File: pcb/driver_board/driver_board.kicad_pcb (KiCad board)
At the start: 2 copper layers, 33 parts

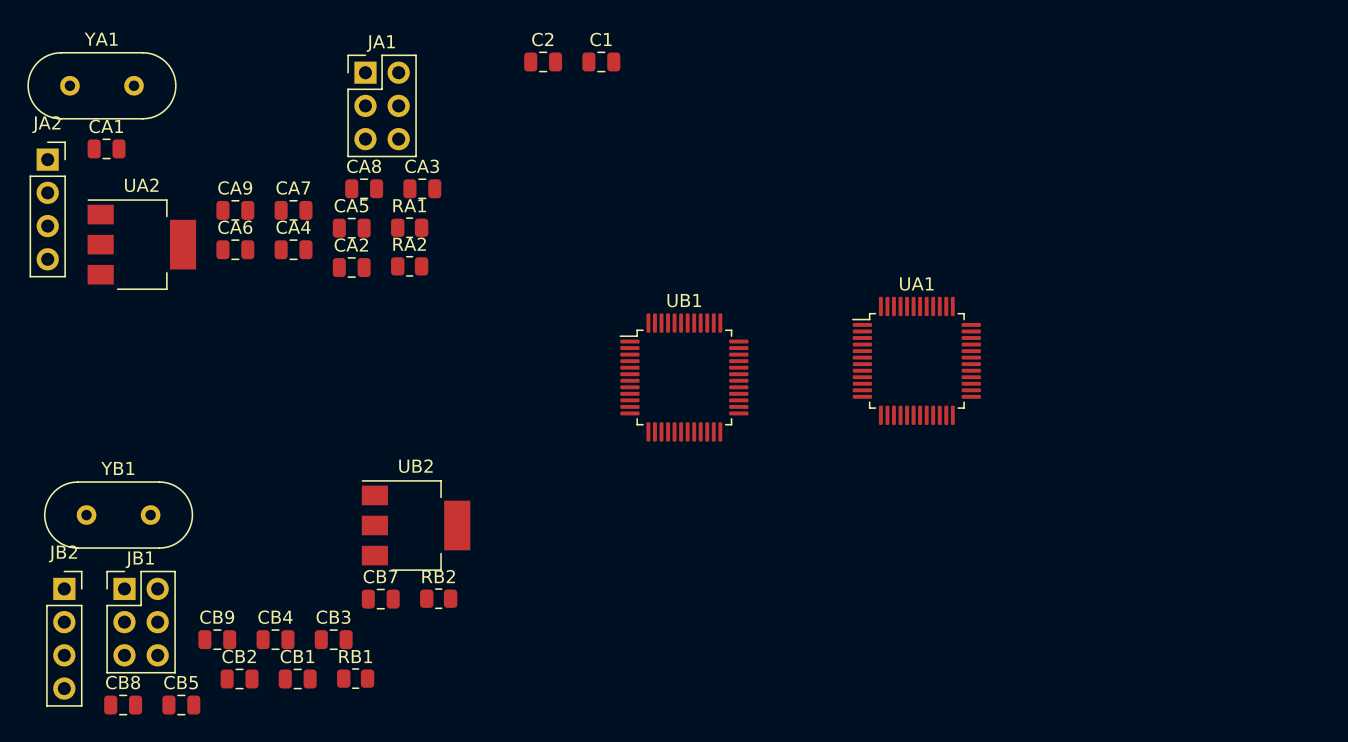
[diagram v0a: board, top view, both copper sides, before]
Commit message: Update Power supply scheme.
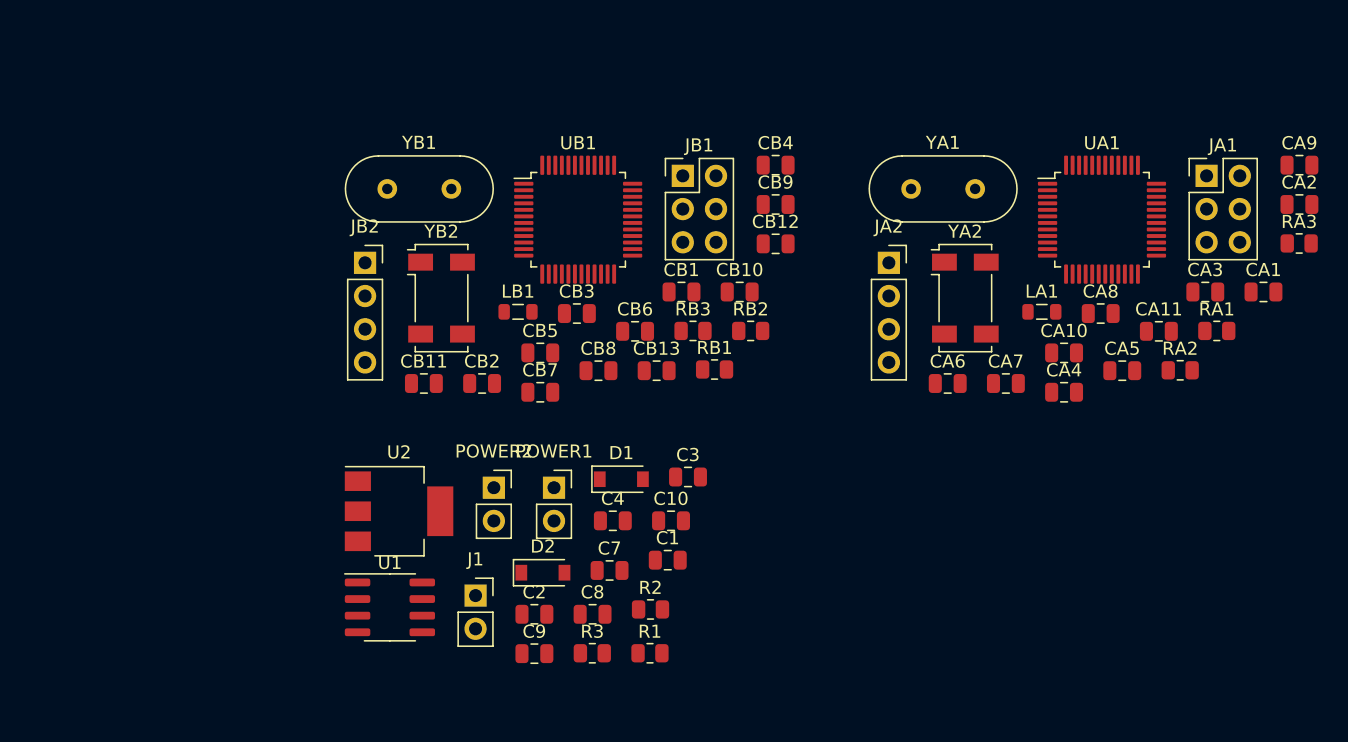
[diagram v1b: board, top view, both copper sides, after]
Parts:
- removed UA2, UB2: AMS1117-3.3, Package_TO_SOT_SMD:SOT-223-3_TabPin2
- added C10: 0.1uF, Capacitor_SMD:C_0805_2012Metric, F.Cu at (100.6, 80.8)
- added C3: 22pF, Capacitor_SMD:C_0805_2012Metric, F.Cu at (101.9, 77.5)
- added C4: 22pF, Capacitor_SMD:C_0805_2012Metric, F.Cu at (96.1, 80.8)
- added C7: 10uF, Capacitor_SMD:C_0805_2012Metric, F.Cu at (95.9, 84.6)
- added C8: 0.1uF, Capacitor_SMD:C_0805_2012Metric, F.Cu at (94.6, 88.0)
- added C9: 10uF, Capacitor_SMD:C_0805_2012Metric, F.Cu at (90.1, 91.0)
- added CA10: 20pF, Capacitor_SMD:C_0805_2012Metric, F.Cu at (130.6, 68.0)
- added CA11: 20pF, Capacitor_SMD:C_0805_2012Metric, F.Cu at (137.9, 66.3)
- added CB10: 20pF, Capacitor_SMD:C_0805_2012Metric, F.Cu at (105.8, 63.3)
- added CB11: 20pF, Capacitor_SMD:C_0805_2012Metric, F.Cu at (81.7, 70.3)
- added CB12: 1uF, Capacitor_SMD:C_0805_2012Metric, F.Cu at (108.6, 59.6)
- added CB13: 10nF, Capacitor_SMD:C_0805_2012Metric, F.Cu at (99.5, 69.3)
- added CB6: 0.1uF, Capacitor_SMD:C_0805_2012Metric, F.Cu at (97.8, 66.3)
- added D1: 1N5817, Diode_SMD:D_SOD-123, F.Cu at (96.8, 77.6)
- added D2: 1N5817, Diode_SMD:D_SOD-123, F.Cu at (90.8, 84.8)
- added J1: Conn_01x02, Connector_PinSocket_2.54mm:PinSocket_1x02_P2.54mm_Vertical, F.Cu at (85.6, 86.5)
- added LA1: 10uH, Inductor_SMD:L_0805_2012Metric, F.Cu at (128.9, 64.8)
- added LB1: 10uH, Inductor_SMD:L_0805_2012Metric, F.Cu at (88.9, 64.8)
- added POWER1: Conn_01x02, Connector_PinSocket_2.54mm:PinSocket_1x02_P2.54mm_Vertical, F.Cu at (91.6, 78.3)
- added POWER2: Conn_01x02, Connector_PinSocket_2.54mm:PinSocket_1x02_P2.54mm_Vertical, F.Cu at (87.0, 78.3)
- added R1: 33R, Resistor_SMD:R_0805_2012Metric, F.Cu at (99.0, 90.9)
- added R2: 33R, Resistor_SMD:R_0805_2012Metric, F.Cu at (99.0, 87.6)
- added R3: 120R, Resistor_SMD:R_0805_2012Metric, F.Cu at (94.6, 90.9)
- added RA3: 0R, Resistor_SMD:R_0805_2012Metric, F.Cu at (148.6, 59.6)
- added RB3: 0R, Resistor_SMD:R_0805_2012Metric, F.Cu at (102.3, 66.3)
- added U1: TJA1051T, Package_SO:SOIC-8_3.9x4.9mm_P1.27mm, F.Cu at (79.1, 87.4)
- added U2: AMS1117-3.3, Package_TO_SOT_SMD:SOT-223-3_TabPin2, F.Cu at (79.8, 80.1)
- added YA2: 32768HZ, Crystal:Crystal_SMD_Abracon_ABS25-4Pin_8.0x3.8mm, F.Cu at (123.1, 63.8)
- added YB2: 32768HZ, Crystal:Crystal_SMD_Abracon_ABS25-4Pin_8.0x3.8mm, F.Cu at (83.0, 63.8)
- CA1: value 10uF -> 4.7uF
- CA2: value 0.1uF -> 10nF
- CA6: value 0.1uF -> 1uF
- CB1: value 10uF -> 0.1uF
- CB2: value 0.1uF -> 4.7uF
- YB1: value 8M -> 8MHZ
- moved CA1 89.2 mm to (145.9, 63.3)
- moved CA9 81.5 mm to (148.6, 53.6)
- moved CA2 72.6 mm to (148.6, 56.6)
- moved JA1 64.8 mm to (141.5, 54.4)
- moved JA2 64.8 mm to (117.2, 61.1)
- moved YA1 64.8 mm to (118.9, 55.4)
- moved RA1 62.2 mm to (142.3, 66.3)
- moved CA3 60.4 mm to (141.4, 63.3)
- moved CA5 59.9 mm to (135.1, 69.3)
- moved CA4 59.9 mm to (130.6, 71.0)
- moved RA2 59.5 mm to (139.5, 69.3)
- moved CA8 57.1 mm to (133.4, 65.0)
- moved CA7 56.1 mm to (126.2, 70.3)
- moved CA6 55.4 mm to (121.7, 70.3)
- moved CB9 54.1 mm to (108.6, 56.6)
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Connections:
- net /Sheet6121200E/OSC_IN renamed /Sheet6121200E/RCC_OSC_IN
- net /Sheet6121200E/OSC_OUT renamed /Sheet6121200E/RCC_OSC_OUT
- net /Sheet6121200E/SWCL renamed /Sheet6121200E/SYS_JTCK-SWCL
- net /Sheet6121200E/SWDIO renamed /Sheet6121200E/SYS_JTMS-SWDIO
- net /sheet61233186/OSC_IN renamed /sheet61233186/RCC_OSC_IN
- net /sheet61233186/OSC_OUT renamed /sheet61233186/RCC_OSC_OUT
- net /sheet61233186/SWCL renamed /sheet61233186/SYS_JTCK-SWCL
- net /sheet61233186/SWDIO renamed /sheet61233186/SYS_JTMS-SWDIO
- net Net-(UA1-Pad42) renamed /Sheet6121200E/USART1_TX
- net Net-(UA1-Pad43) renamed /Sheet6121200E/USART1_RX
- net VCC renamed +5V
- CA1 pad 1: /Sheet6121200E/V3.3 -> /Sheet6121200E/VDD1
- CA2 pad 1: /Sheet6121200E/V3.3 -> +3.3VA
- CA3 pad 1: /Sheet6121200E/V3.3 -> /Sheet6121200E/VDD1
- CA4 pad 1: /Sheet6121200E/V3.3 -> /Sheet6121200E/VDD1
- CA5 pad 1: /Sheet6121200E/V3.3 -> /Sheet6121200E/VDD1
- CA6 pad 1: /Sheet6121200E/V3.3 -> +3.3VA
- CA9 pad 1: /Sheet6121200E/V3.3 -> +3.3V
- CB1 pad 1: /sheet61233186/V3.3 -> /sheet61233186/VDD1
- CB2 pad 1: /sheet61233186/V3.3 -> /sheet61233186/VDD2
- CB3 pad 1: /sheet61233186/V3.3 -> +3.3V
- CB4 pad 1: /sheet61233186/V3.3 -> +3.3V
- CB5 pad 1: /sheet61233186/V3.3 -> +3.3V
- CB9 pad 1: /sheet61233186/V3.3 -> +3.3V
- JA1 pad 1: /Sheet6121200E/V3.3 -> +3.3V
- JA1 pad 2: /Sheet6121200E/V3.3 -> +3.3V
- JA2 pad 4: /Sheet6121200E/V3.3 -> +3.3V
- JB1 pad 1: /sheet61233186/V3.3 -> +3.3V
- JB1 pad 2: /sheet61233186/V3.3 -> +3.3V
- JB2 pad 4: /sheet61233186/V3.3 -> +3.3V
- UA1 pad 12: Net-(UA1-Pad12) -> /sheet61233186/F031_RX
- UA1 pad 13: Net-(UA1-Pad13) -> /sheet61233186/F031_TX
- UA1 pad 24: /Sheet6121200E/V3.3 -> /Sheet6121200E/VDD1
- UA1 pad 3: Net-(UA1-Pad3) -> /Sheet6121200E/RCC_OSC32_IN
- UA1 pad 30: /sheet61233186/F031_RX -> Net-(UA1-Pad30)
- UA1 pad 31: /sheet61233186/F031_TX -> Net-(UA1-Pad31)
- UA1 pad 36: /Sheet6121200E/V3.3 -> /Sheet6121200E/VDD1
- UA1 pad 4: Net-(UA1-Pad4) -> /Sheet6121200E/RCC_OSC32_OUT
- UA1 pad 45: Net-(UA1-Pad45) -> CAN_RX
- UA1 pad 46: Net-(UA1-Pad46) -> CAN_TX
- UA1 pad 48: /Sheet6121200E/V3.3 -> /Sheet6121200E/VDD1
- UA1 pad 8: GND -> GNDA
- UA1 pad 9: /Sheet6121200E/V3.3 -> +3.3VA
- UB1 pad 24: /sheet61233186/V3.3 -> /sheet61233186/VDD1
- UB1 pad 3: Net-(UB1-Pad3) -> /sheet61233186/RCC_OSC32_IN
- UB1 pad 4: Net-(UB1-Pad4) -> /sheet61233186/RCC_OSC32_OUT
- UB1 pad 48: /sheet61233186/V3.3 -> /sheet61233186/VDD2
- UB1 pad 8: GND -> GNDA
- UB1 pad 9: /sheet61233186/V3.3 -> +3.3VA

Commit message: Update layout.
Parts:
- removed CA1: 4.7uF, Capacitor_SMD:C_0805_2012Metric
- removed CA10, CA11, CA7, CA8, CB11: 20pF, Capacitor_SMD:C_0805_2012Metric
- removed CA2, CB13: 10nF, Capacitor_SMD:C_0805_2012Metric
- removed CA3, CA4, CA5, CA9: 0.1uF, Capacitor_SMD:C_0805_2012Metric
- removed CA6, CB12: 1uF, Capacitor_SMD:C_0805_2012Metric
- removed J1: Conn_01x02, Connector_PinSocket_2.54mm:PinSocket_1x02_P2.54mm_Vertical
- removed JA1: Conn_02x03_Odd_Even, Connector_PinHeader_2.54mm:PinHeader_2x03_P2.54mm_Vertical
- removed JA2: Conn_01x04, Connector_PinSocket_2.54mm:PinSocket_1x04_P2.54mm_Vertical
- removed LA1: 10uH, Inductor_SMD:L_0805_2012Metric
- removed RA1, RA2: 100K, Resistor_SMD:R_0805_2012Metric
- removed RA3: 0R, Resistor_SMD:R_0805_2012Metric
- removed UA1: STM32F103C6Tx, Package_QFP:LQFP-48_7x7mm_P0.5mm
- removed YA1: 8M, Crystal:Crystal_HC18-U_Vertical
- removed YA2: 32768HZ, Crystal:Crystal_SMD_Abracon_ABS25-4Pin_8.0x3.8mm
- added C11: 10pF, Capacitor_SMD:C_0805_2012Metric, F.Cu at (83.8, 129.9)
- added CAN1: Conn_01x02, Connector_Phoenix_MC:PhoenixContact_MCV_1,5_2-G-3.81_1x02_P3.81mm_Vertical, F.Cu at (119.4, 132.7)
- added LED1: LED, LED_SMD:LED_0805_2012Metric, F.Cu at (99.7, 126.0)
- added Motor1: Conn_01x05, Connector_PinHeader_2.54mm:PinHeader_1x05_P2.54mm_Vertical, F.Cu at (78.7, 43.2)
- added Motor2: Conn_01x05, Connector_PinHeader_2.54mm:PinHeader_1x05_P2.54mm_Vertical, F.Cu at (78.7, 58.4)
- added Motor3: Conn_01x05, Connector_PinHeader_2.54mm:PinHeader_1x05_P2.54mm_Vertical, F.Cu at (78.7, 73.7)
- added R4: 10K, Resistor_SMD:R_0805_2012Metric, F.Cu at (80.6, 127.9)
- added R5: 510R, Resistor_SMD:R_0805_2012Metric, F.Cu at (99.7, 122.2)
- added SW1: SW_Push, Button_Switch_SMD:SW_SPST_B3U-1000P, F.Cu at (80.6, 132.5)
- CB1, CB2, CB3, LB1, RB3: moved to B.Cu
- CB4: value 0.1uF -> 1uF; moved to B.Cu
- CB5: value 0.1uF -> 10nF; moved to B.Cu
- CB6, CB9: value 0.1uF -> 20pF
- CB8: value 20pF -> 0.1uF
- POWER1, POWER2: footprint Connector_PinSocket_2.54mm:PinSocket_1x02_P2.54mm_Vertical -> Connector_Phoenix_MC:PhoenixContact_MCV_1,5_2-G-3.81_1x02_P3.81mm_Vertical
- moved POWER1 56.2 mm to (105.4, 132.7)
- moved POWER2 54.5 mm to (89.5, 132.7)
- moved RB2 54.3 mm to (157.8, 84.5)
- moved CB6 52.8 mm to (147.8, 83.2)
- moved D2 51.4 mm to (124.2, 123.8), turned to 180 degrees
- moved D1 51.0 mm to (118.4, 123.8)
- moved CB8 50.5 mm to (141.5, 89.2)
- moved RB1 46.5 mm to (145.9, 89.2)
- moved YB2 46.5 mm to (125.0, 83.7)
- moved YB1 45.8 mm to (124.5, 50.8)
- moved U1 45.6 mm to (121.3, 104.8), turned to 270 degrees
- moved CB10 44.8 mm to (144.3, 86.2)
- moved U2 43.9 mm to (107.3, 114.3), turned to 90 degrees
- moved C4 43.8 mm to (123.2, 115.2), turned to 270 degrees
- moved CB9 43.3 mm to (137.0, 89.2)
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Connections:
- C4 pad 1: /CANL -> /CANH
- C7 pad 2: GND -> GNDA
- C8 pad 2: GND -> GNDA
- CB1 pad 1: /sheet61233186/VDD1 -> +3.3V
- CB10 pad 2: /sheet61233186/RCC_OSC32_IN -> /sheet61233186/RCC_OSC32_OUT
- CB2 pad 1: /sheet61233186/VDD2 -> +3.3V
- CB4 pad 1: +3.3V -> +3.3VA
- CB5 pad 1: +3.3V -> +3.3VA
- CB6 pad 1: /sheet61233186/VDD2 -> Net-(CB6-Pad1)
- CB6 pad 2: GND -> /sheet61233186/RCC_OSC_IN
- CB7 pad 1: Net-(CB7-Pad1) -> Net-(CB6-Pad1)
- CB7 pad 2: /sheet61233186/RCC_OSC_IN -> /sheet61233186/RCC_OSC_OUT
- CB8 pad 1: Net-(CB7-Pad1) -> +3.3V
- CB8 pad 2: /sheet61233186/RCC_OSC_OUT -> Net-(CB8-Pad2)
- CB9 pad 1: +3.3V -> Net-(CB10-Pad1)
- CB9 pad 2: GND -> /sheet61233186/RCC_OSC32_IN
- JB2 pad 1: GND -> Net-(CB8-Pad2)
- POWER2 pad 1: GND -> GNDA
- UB1 pad 11: Net-(UB1-Pad11) -> /sheet61233186/TIM2_CH2
- UB1 pad 13: Net-(UB1-Pad13) -> /sheet61233186/TIM2_CH4
- UB1 pad 15: Net-(UB1-Pad15) -> /sheet61233186/TIM2_CH1
- UB1 pad 18: Net-(UB1-Pad18) -> /sheet61233186/TIM3_CH3
- UB1 pad 19: Net-(UB1-Pad19) -> /sheet61233186/TIM3_CH4
- UB1 pad 21: Net-(UB1-Pad21) -> /sheet61233186/TIM2_CH3
- UB1 pad 24: /sheet61233186/VDD1 -> +3.3V
- UB1 pad 29: Net-(UB1-Pad29) -> /sheet61233186/TIM1_CH1
- UB1 pad 30: Net-(UB1-Pad30) -> /sheet61233186/TIM1_CH2
- UB1 pad 31: Net-(UB1-Pad31) -> /sheet61233186/TIM1_CH3
- UB1 pad 32: Net-(UB1-Pad32) -> /sheet61233186/TIM1_CH4
- UB1 pad 40: Net-(UB1-Pad40) -> /sheet61233186/TIM3_CH1
- UB1 pad 41: Net-(UB1-Pad41) -> /sheet61233186/TIM3_CH2
- UB1 pad 48: /sheet61233186/VDD2 -> +3.3V
- UB1 pad 7: Net-(UB1-Pad7) -> RESET
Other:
- board outline added: 99.1 x 99.1 mm

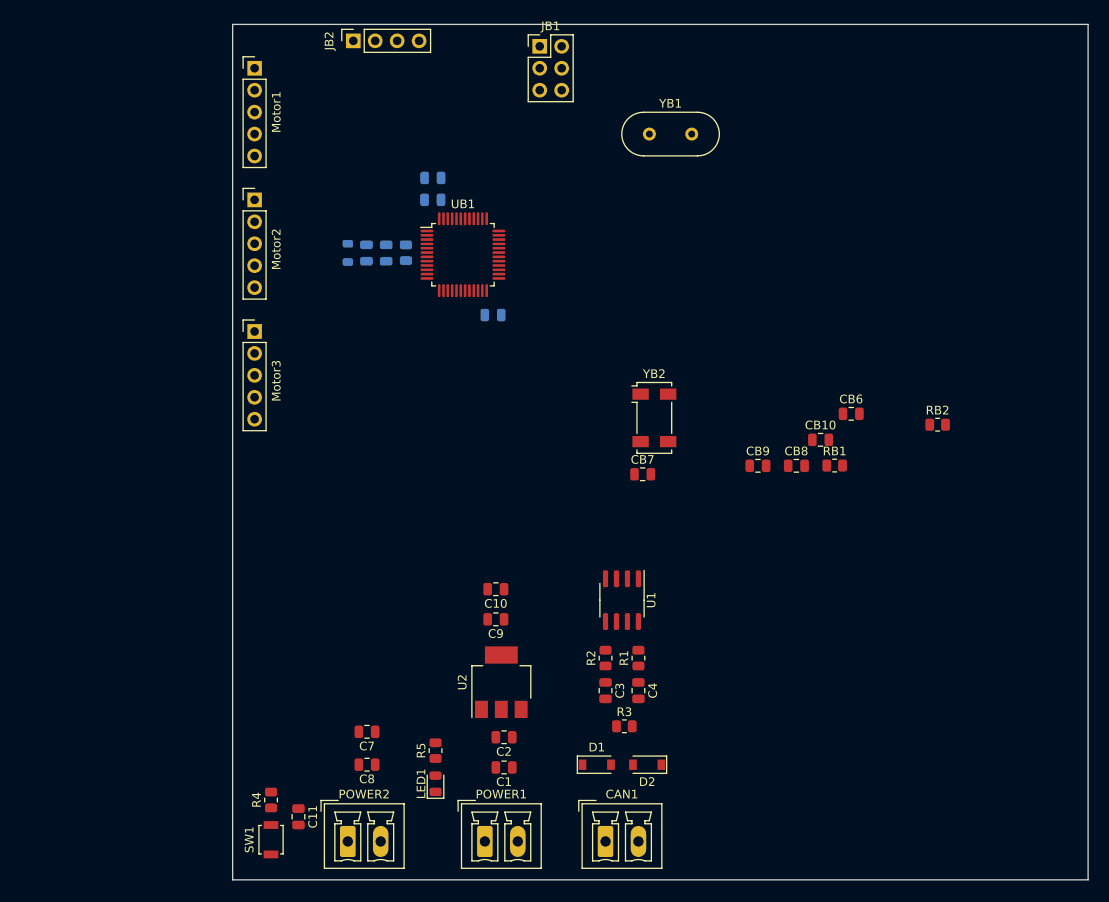
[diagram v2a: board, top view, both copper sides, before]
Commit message: Complete the driver_board.
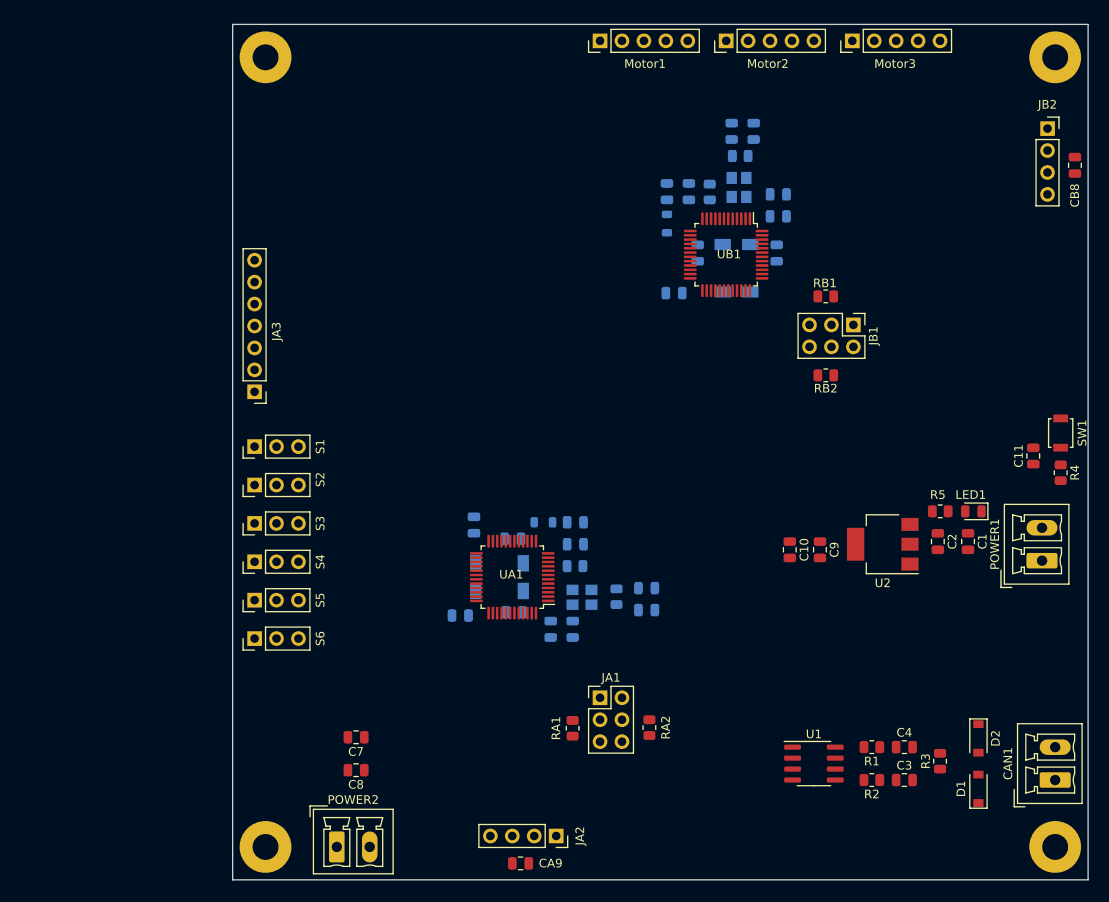
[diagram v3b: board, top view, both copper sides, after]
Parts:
- added CA1: 4.7uF, Capacitor_SMD:C_0805_2012Metric, B.Cu at (115.6, 108.1)
- added CA10: 20pF, Capacitor_SMD:C_0805_2012Metric, B.Cu at (108.8, 106.2)
- added CA11: 20pF, Capacitor_SMD:C_0805_2012Metric, B.Cu at (108.6, 97.7)
- added CA2: 10nF, Capacitor_SMD:C_0805_2012Metric, B.Cu at (115.9, 98.3)
- added CA3: 0.1uF, Capacitor_SMD:C_0805_2012Metric, B.Cu at (104.1, 96.1)
- added CA4: 0.1uF, Capacitor_SMD:C_0805_2012Metric, B.Cu at (102.6, 106.6)
- added CA5: 0.1uF, Capacitor_SMD:C_0805_2012Metric, B.Cu at (113.0, 108.1)
- added CA6: 1uF, Capacitor_SMD:C_0805_2012Metric, B.Cu at (115.9, 95.8)
- added CA7: 20pF, Capacitor_SMD:C_0805_2012Metric, B.Cu at (124.1, 105.9)
- added CA8: 20pF, Capacitor_SMD:C_0805_2012Metric, B.Cu at (124.1, 103.4)
- added CA9: 0.1uF, Capacitor_SMD:C_0805_2012Metric, F.Cu at (109.5, 135.3)
- added JA1: Conn_02x03_Odd_Even, Connector_PinHeader_2.54mm:PinHeader_2x03_P2.54mm_Vertical, F.Cu at (118.7, 116.1)
- added JA2: Conn_01x04, Connector_PinSocket_2.54mm:PinSocket_1x04_P2.54mm_Vertical, F.Cu at (113.7, 132.1)
- added JA3: Conn_01x07, Connector_PinHeader_2.54mm:PinHeader_1x07_P2.54mm_Vertical, F.Cu at (78.7, 80.6)
- added LA1: 10uH, Inductor_SMD:L_0805_2012Metric, B.Cu at (112.2, 95.8)
- added Pad1: MountingHole_3mm_Pad, MountingHole:MountingHole_3mm_Pad, F.Cu at (80.0, 41.9)
- added Pad2: MountingHole_3mm_Pad, MountingHole:MountingHole_3mm_Pad, F.Cu at (171.4, 41.9)
- added Pad3: MountingHole_3mm_Pad, MountingHole:MountingHole_3mm_Pad, F.Cu at (80.0, 133.3)
- added Pad4: MountingHole_3mm_Pad, MountingHole:MountingHole_3mm_Pad, F.Cu at (171.4, 133.3)
- added RA1: 100K, Resistor_SMD:R_0805_2012Metric, F.Cu at (115.6, 119.6)
- added RA2: 100K, Resistor_SMD:R_0805_2012Metric, F.Cu at (124.5, 119.5)
- added RA3: 0R, Resistor_SMD:R_0805_2012Metric, B.Cu at (115.8, 100.8)
- added RA4: 10M, Resistor_SMD:R_0805_2012Metric, B.Cu at (120.7, 104.4)
- added RB4: 10M, Resistor_SMD:R_0805_2012Metric, B.Cu at (135.0, 53.3)
- added S1: Conn_01x03, Connector_PinHeader_2.54mm:PinHeader_1x03_P2.54mm_Vertical, F.Cu at (78.7, 87.0)
- added S2: Conn_01x03, Connector_PinHeader_2.54mm:PinHeader_1x03_P2.54mm_Vertical, F.Cu at (78.7, 91.4)
- added S3: Conn_01x03, Connector_PinHeader_2.54mm:PinHeader_1x03_P2.54mm_Vertical, F.Cu at (78.7, 95.9)
- added S4: Conn_01x03, Connector_PinHeader_2.54mm:PinHeader_1x03_P2.54mm_Vertical, F.Cu at (78.7, 100.3)
- added S5: Conn_01x03, Connector_PinHeader_2.54mm:PinHeader_1x03_P2.54mm_Vertical, F.Cu at (78.7, 104.8)
- added S6: Conn_01x03, Connector_PinHeader_2.54mm:PinHeader_1x03_P2.54mm_Vertical, F.Cu at (78.7, 109.2)
- added UA1: STM32F103C6Tx, Package_QFP:LQFP-48_7x7mm_P0.5mm, F.Cu at (108.6, 102.1)
- added YA1: 8M, Crystal:Crystal_SMD_Abracon_ABM8G-4Pin_3.2x2.5mm, B.Cu at (116.7, 104.4)
- added YA2: 32768HZ, Crystal:Crystal_SMD_Abracon_ABS25-4Pin_8.0x3.8mm, B.Cu at (107.1, 102.1)
- CB10, CB6, CB7, CB9, YB2: moved to B.Cu
- YB1: value 8MHZ -> 8M; footprint Crystal:Crystal_HC18-U_Vertical -> Crystal:Crystal_SMD_Abracon_ABM8G-4Pin_3.2x2.5mm; moved to B.Cu
- moved SW1 102.9 mm to (172.1, 85.4), turned to 270 degrees
- moved R4 99.0 mm to (172.1, 90.0), turned to 270 degrees
- moved C11 94.8 mm to (168.9, 88.1), turned to 90 degrees
- moved JB2 81.0 mm to (170.6, 50.2), turned to 0 degrees
- moved Motor3 77.0 mm to (148.0, 40.0), turned to 90 degrees
- moved POWER1 72.2 mm to (169.9, 100.2), turned to 90 degrees
- moved LED1 69.8 mm to (162.0, 94.5), turned to 180 degrees
- moved R5 64.7 mm to (158.1, 94.5), turned to 180 degrees
- moved C1 59.8 mm to (161.4, 98.0), turned to 270 degrees
- moved Motor2 57.6 mm to (133.3, 40.0), turned to 90 degrees
- moved C2 55.1 mm to (157.9, 98.0), turned to 270 degrees
- moved CAN1 52.6 mm to (171.4, 125.6), turned to 90 degrees
- moved JB1 48.6 mm to (148.1, 72.9), turned to 270 degrees
- moved CB8 47.4 mm to (173.7, 54.4), turned to 90 degrees
- moved U2 47.0 mm to (151.5, 98.3), turned to 180 degrees
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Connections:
- net +3.3VA renamed /sheet61233186/3.3VA
- CB10 pad 1: Net-(CB10-Pad1) -> GND
- CB6 pad 1: Net-(CB6-Pad1) -> GND
- CB7 pad 1: Net-(CB6-Pad1) -> GND
- CB8 pad 2: Net-(CB8-Pad2) -> GND
- CB9 pad 1: Net-(CB10-Pad1) -> GND
- JB2 pad 1: Net-(CB8-Pad2) -> GND
- YB1 pad 2: /sheet61233186/RCC_OSC_OUT -> Net-(YB1-Pad2)
